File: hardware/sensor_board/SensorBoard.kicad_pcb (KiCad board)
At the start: 2 copper layers, 156.9 x 102.2 mm, 77 parts, among them J1 Relay Board, J10 GND BUS, J11 FEED SENSOR R, J13 SPARE GPIO, J15 LED L1, J16 LED L2, J17 LED L3, J18 LED L4, J19 LED R1, J2 Pi, J20 EXT, J21 LED R2, J22 LED R3, J23 LED R4, J24 Raspberry Pi GPIO header, J25 RTC Header, J26 I2C0, J27 I2C1, J28 I2C2, J29 I2C3, J3 Display, J30 I2C4, J31 I2C5, J32 I2C6, J33 I2C7, J4 DC IN 5V, J5 VSYS BUS, J6 SOIL SENSOR L, J7 3V3 BUS, J8 FEED SENSOR L, J9 SOIL SENSOR R, Q1 PN2222A, Q2 PN2222A, Q3 PN2222A, Q4 PN2222A, Q5 PN2222A, Q6 PN2222A, Q7 PN2222A, Q8 PN2222A, SW1 Reset, U1 Raspberry Pico, U2 74HC595, U3 TCA9548A, U4 LM1117, U5 DS3231MZ, U6 74HC165

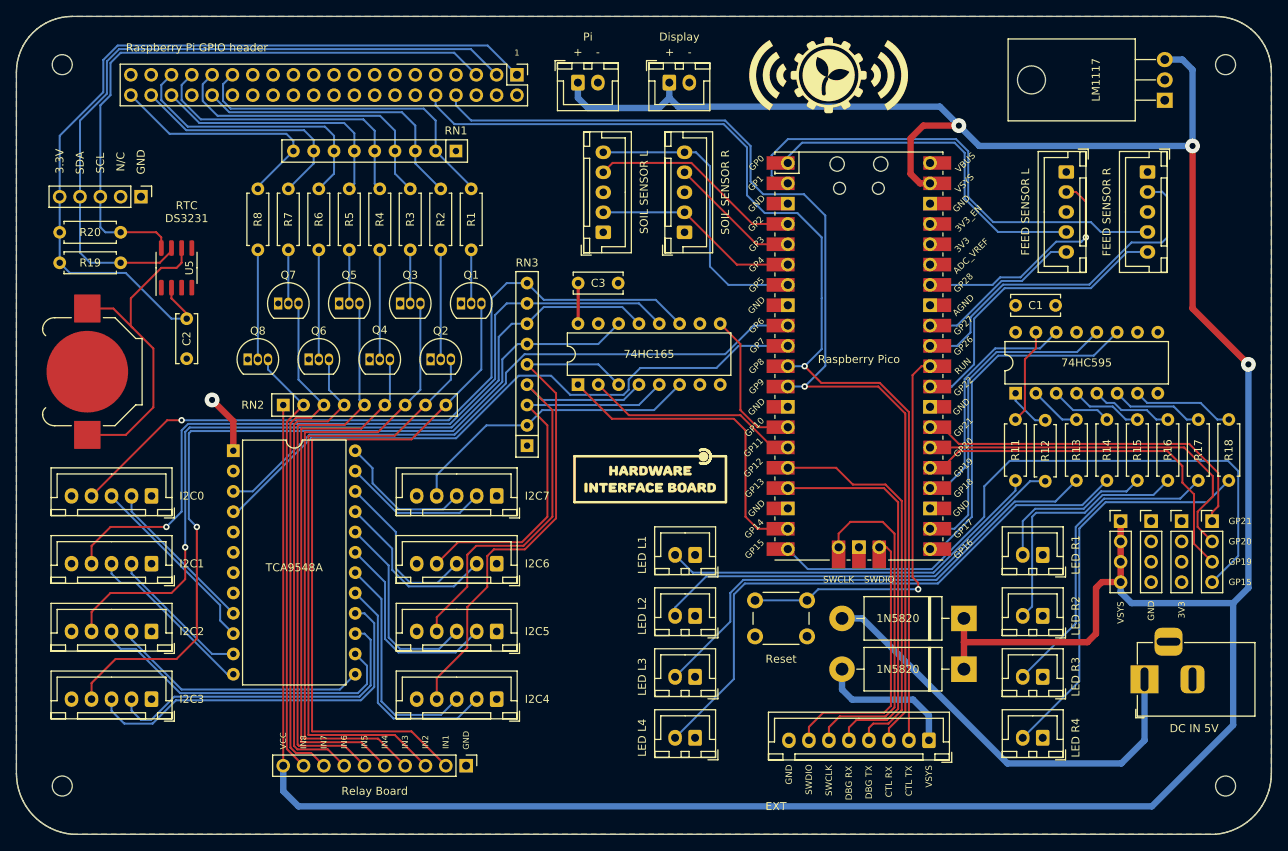
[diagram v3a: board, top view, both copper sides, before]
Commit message: Completely revamped board. Will fully use the I2C expander now to have one "sensor pod" per grow system containing an SCD30 and a soil sensor. This allows for 8 sensor pods. Will reuse the I2C interface for the soil sensors for additional feed level sonar sensors.
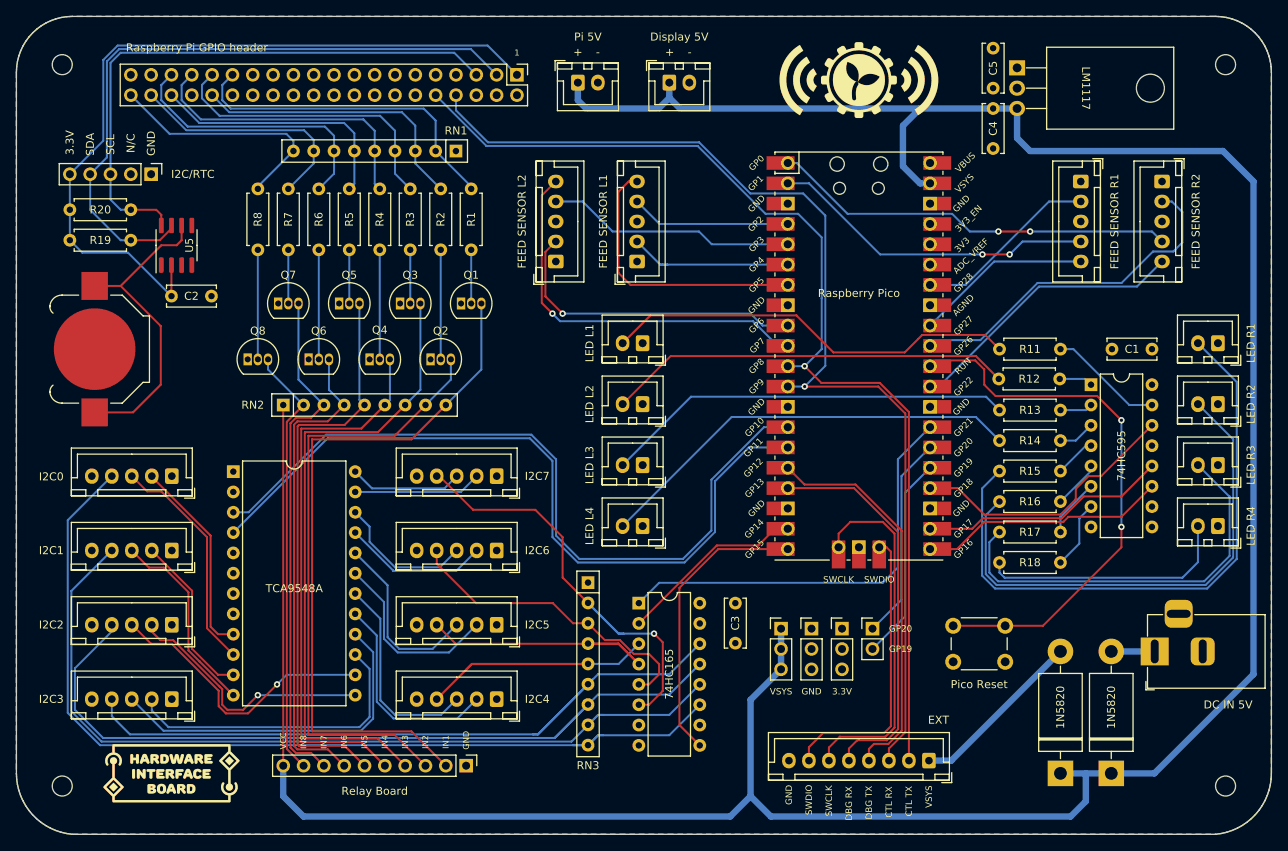
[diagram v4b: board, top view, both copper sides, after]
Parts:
- added C4: 10uf, Capacitor_THT:C_Disc_D6.0mm_W2.5mm_P5.00mm, F.Cu at (189.7, 54.3)
- added C5: 10uf, Capacitor_THT:C_Disc_D6.0mm_W2.5mm_P5.00mm, F.Cu at (189.7, 46.8)
- J10, J5, J7: footprint Connector_PinHeader_2.54mm:PinHeader_1x04_P2.54mm_Vertical -> Connector_PinHeader_2.54mm:PinHeader_1x03_P2.54mm_Vertical
- J11: value FEED SENSOR R -> FEED SENSOR R2
- J13: footprint Connector_PinHeader_2.54mm:PinHeader_1x04_P2.54mm_Vertical -> Connector_PinHeader_2.54mm:PinHeader_1x02_P2.54mm_Vertical
- J2: value Pi -> Pi 5V
- J3: value Display -> Display 5V
- J6: value SOIL SENSOR L -> FEED SENSOR L1
- J8: value FEED SENSOR L -> FEED SENSOR R1
- J9: value SOIL SENSOR R -> FEED SENSOR L2
- SW1: value Reset -> Pico Reset
- moved C3 44.6 mm to (157.5, 111.1), turned to -90 degrees
- moved J10 44.5 mm to (167.0, 114.3)
- moved J5 44.5 mm to (163.2, 114.3)
- moved J13 44.5 mm to (174.6, 114.3)
- moved J7 44.5 mm to (170.8, 114.3)
- moved J19 34.4 mm to (217.8, 78.6)
- moved J21 34.4 mm to (217.8, 86.2)
- moved J22 34.4 mm to (217.8, 93.9)
- moved J23 34.4 mm to (217.8, 101.5)
- moved U6 28.4 mm to (145.4, 111.1), turned to 0 degrees
- moved R18 27.6 mm to (198.1, 106.0), turned to 180 degrees
- moved J15 27.3 mm to (145.9, 78.6)
- moved J16 27.3 mm to (145.9, 86.2)
- moved J17 27.3 mm to (145.9, 93.9)
- moved J18 27.3 mm to (145.9, 101.5)
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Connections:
- net /FEED SENSOR L RX renamed /FEED SENSOR R1 RX
- net /FEED SENSOR L TX renamed /FEED SENSOR R1 TX
- net /FEED SENSOR R RX renamed /FEED SENSOR R2 RX
- net /FEED SENSOR R TX renamed /FEED SENSOR R2 TX
- net /SOIL SENSOR L DETECT renamed /FEED SENSOR L1 DETECT
- net /SOIL SENSOR R DETECT renamed /FEED SENSOR L2 DETECT
- J11 pad 4: /FEED SENSOR R DETECT -> /FEED SENSOR R2 DETECT
- J13 pad 1: /GPIO21 -> /GPIO20
- J13 pad 2: /GPIO20 -> /GPIO19
- J4 pad 3: (no net) -> unconnected-(J4-Pad3)
- J6 pad 2: Net-(U1-Pad6) -> /FEED SENSOR L1 TX
- J6 pad 5: Net-(U1-Pad7) -> /FEED SENSOR L1 RX
- J8 pad 4: /FEED SENSOR L DETECT -> /FEED SENSOR R1 DETECT
- J9 pad 2: Net-(U1-Pad6) -> /FEED SENSOR L2 TX
- J9 pad 5: Net-(U1-Pad7) -> /FEED SENSOR L2 RX
- U1 pad 1: /FEED SENSOR L DETECT -> /FEED SENSOR R2 DETECT
- U1 pad 10: /I2C1 SCL -> /FEED SENSOR L2 RX
- U1 pad 14: Net-(U1-Pad14) -> /I2C1 SDA
- U1 pad 15: Net-(U1-Pad15) -> /I2C1 SCL
- U1 pad 2: /FEED SENSOR R DETECT -> /FEED SENSOR R1 DETECT
- U1 pad 20: /GPIO15 -> Net-(U1-Pad20)
- U1 pad 27: /GPIO21 -> Net-(U1-Pad27)
- U1 pad 6: Net-(U1-Pad6) -> /FEED SENSOR L1 TX
- U1 pad 7: Net-(U1-Pad7) -> /FEED SENSOR L1 RX
- U1 pad 9: /I2C1 SDA -> /FEED SENSOR L2 TX
- U6 pad 1: Net-(U1-Pad19) -> Net-(U1-Pad27)
- U6 pad 2: Net-(U1-Pad15) -> Net-(U1-Pad19)
- U6 pad 9: Net-(U1-Pad14) -> Net-(U1-Pad20)
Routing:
- net /GPIO15: track 80.9 -> 0.00 mm
- net /FEED SENSOR R DETECT: track 61.0 -> 0.00 mm
- net Net-(J19-Pad2): track 20.7 -> 77.0 mm
- net Net-(U1-Pad27): track 0.00 -> 53.4 mm
- net /FEED SENSOR R2 DETECT: track 0.00 -> 50.8 mm, vias 0 -> 2
- net /FEED SENSOR L2 RX: track 0.00 -> 48.9 mm, vias 0 -> 1
- net Net-(D2-Pad2): track 54.1 -> 5.43 mm
- net /FEED SENSOR L DETECT: track 44.3 -> 0.00 mm
- net /GPIO21: track 43.2 -> 0.00 mm
- net /FEED SENSOR R1 DETECT: track 0.00 -> 41.0 mm, vias 0 -> 2
- net /FEED SENSOR L2 TX: track 0.00 -> 39.2 mm, vias 0 -> 1
- net Net-(U1-Pad7): track 37.3 -> 0.00 mm
- net VS: track 415.8 -> 378.6 mm, vias 3 -> 0
- net Net-(U1-Pad20): track 0.00 -> 36.3 mm
- net /FEED SENSOR L1 RX: track 0.00 -> 34.8 mm
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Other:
- board text added: "I2C/RTC"
- board text removed: "3V3"
- board text removed: "GP15"
- board text removed: "GP21"
- board text removed: "RTC DS3231"
